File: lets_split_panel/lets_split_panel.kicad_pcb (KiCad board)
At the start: 2 copper layers, 230.5 x 82 mm, 122 parts, among them J1 Speaker, J3 ISP, J5 Speaker, J6 ISP, J7 WS2812>, J8 WS2812>, P2 USB_OTG, P3 >WS2812, P4 Conn_01x04, P5 USB_OTG, P6 >WS2812, P8 Conn_01x04, SW1 Socket, SW10 Socket, SW11 Socket, SW12 Socket, SW13 Socket, SW14 Socket, SW15 Socket, SW16 Socket, SW17 Socket, SW18 Socket, SW19 Socket, SW2 Socket, SW20 Socket, SW21 Socket, SW22 Socket, SW23 Socket, SW24 Socket, SW25 Socket, SW26 Socket, SW27 Socket, SW28 Socket, SW29 Socket, SW3 Socket, SW30 Socket, SW31 Socket, SW32 Socket, SW33 Socket, SW34 Socket, SW35 Socket, SW36 Socket, SW37 Socket, SW38 Socket, SW39 Socket, SW4 Socket, SW40 Socket, SW41 Socket, SW42 Socket, SW43 Socket, SW44 Socket, SW45 Socket, SW46 Socket, SW47 Socket, SW48 Socket, SW5 Socket, SW6 Socket, SW7 Socket, SW8 Socket, SW9 Socket, U1 ATMega32U4, U2 ATMega32U4, Y1 Crystal, Y2 Crystal

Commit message: updated gerbers
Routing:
- net /Right half/col5: track 139.9 -> 140.7 mm

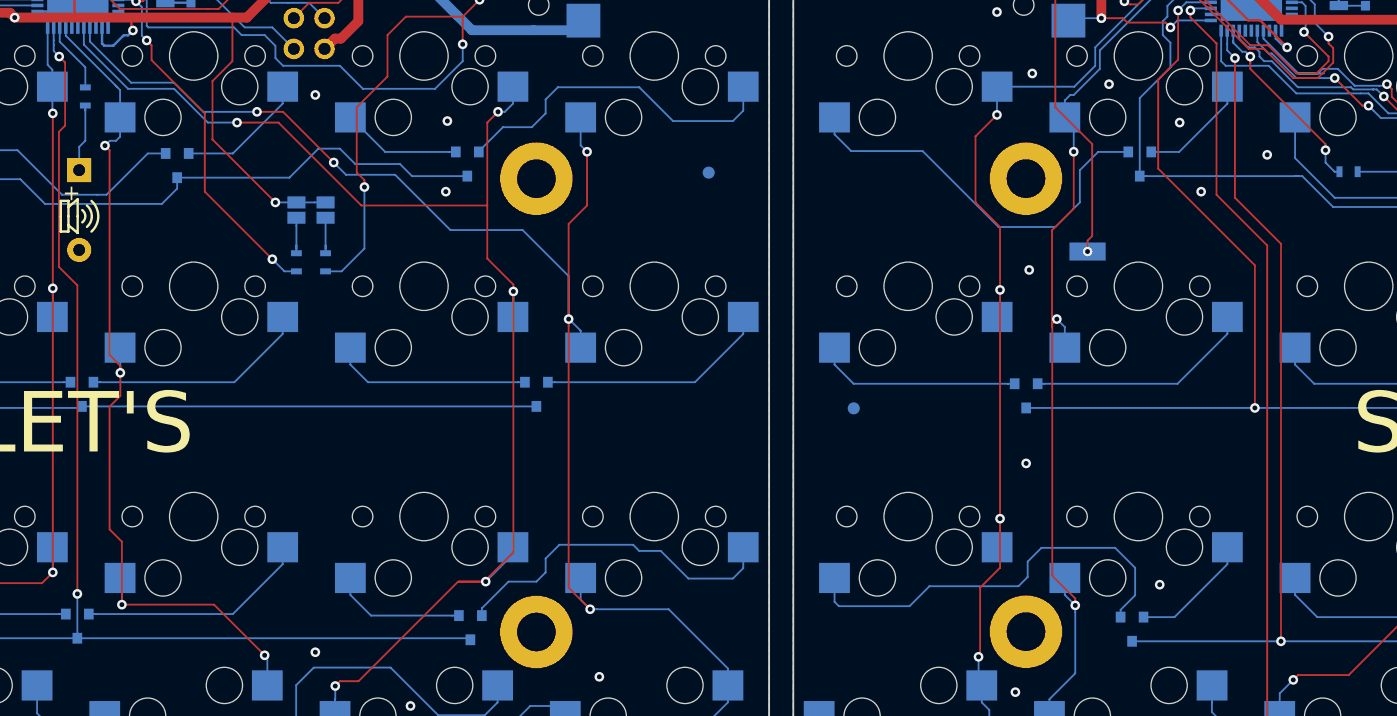
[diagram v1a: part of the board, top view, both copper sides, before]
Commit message: Seperated gerbers on request from board house
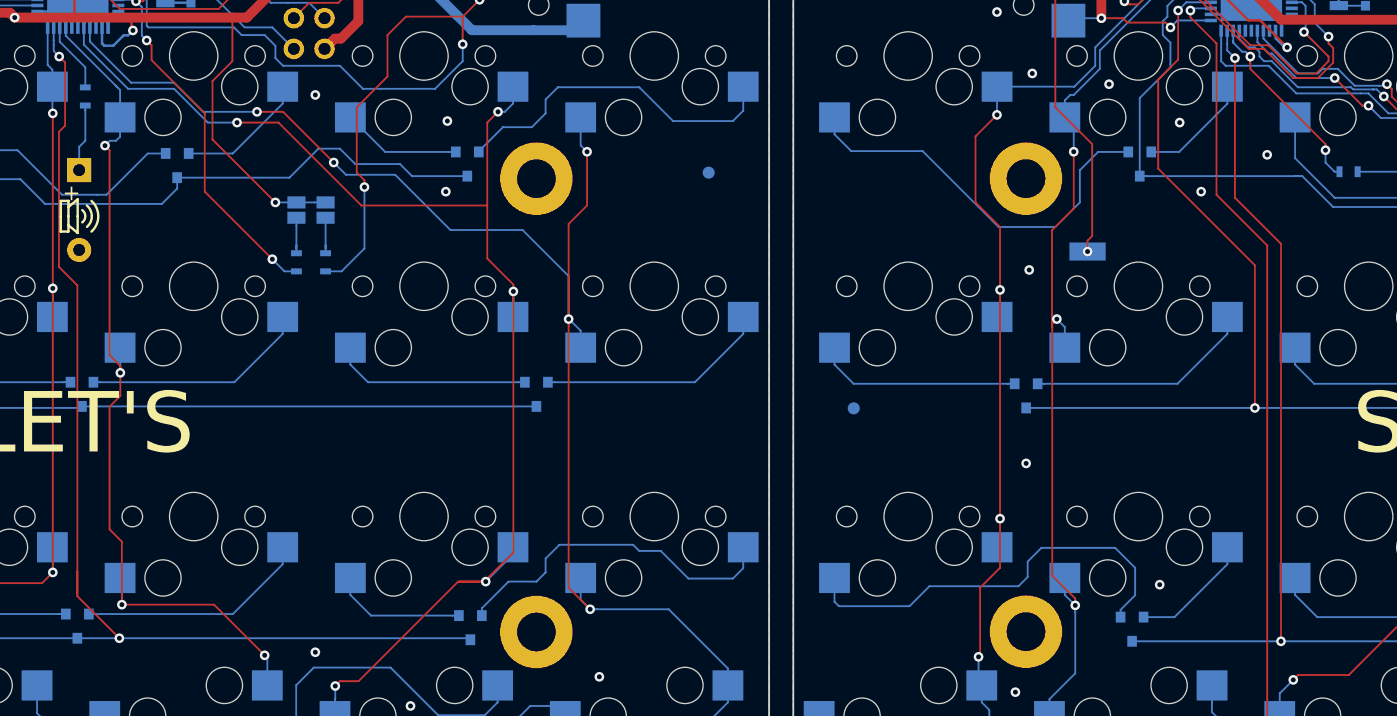
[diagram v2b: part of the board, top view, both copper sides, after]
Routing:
- net /Left half/row2: track 114.1 -> 117.4 mm
- net /Right half/col5: track 140.7 -> 138.6 mm

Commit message: Added PnP files and split gerbers
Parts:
- added FID5: Fiducial, Fiducials:Fiducial_1mm_Dia_2mm_Outer, B.Cu at (143.8, 68.8)
- added FID6: Fiducial, Fiducials:Fiducial_1mm_Dia_2mm_Outer, B.Cu at (27.5, 68.8)
- added G***: LOGO, graphics:kiwi, F.Cu at (203.7, 62.8)
- added G***: LOGO, graphics:kiwi, F.Cu at (67.7, 62.8)
- C2, C3, C6, C7: value 8pF -> 18pF
- FID1, FID2, FID3, FID4: renamed from REF**; value Fiducial_1mm_Dia_2mm_Outer -> Fiducial
- R10, R3: value 200 -> 200R
- Y1, Y2: footprint SeeedOPL-Crystal Oscillator-2016:X2-SMD-3.2X1.5X0.55MM -> Crystals:Crystal_SMD_Abracon_ABM3-2pin_5.0x3.2mm
- moved C6 2.19 mm to (189.8, 68.2)
- moved C7 2.17 mm to (189.8, 65.0)
- moved C2 1.90 mm to (92.0, 68.8)
- moved C3 1.58 mm to (92.0, 64.8)
- moved Y2 1.52 mm to (186.8, 66.5)
- moved Y1 1.03 mm to (89.2, 66.5)
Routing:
- net GND: track 298.2 -> 290.5 mm, vias 41 -> 40
- net Net-(C7-Pad1): track 6.89 -> 10.5 mm
- net Net-(C3-Pad1): track 6.86 -> 9.54 mm
- net Net-(C6-Pad1): track 6.89 -> 8.92 mm
- net Net-(C2-Pad1): track 6.80 -> 8.78 mm
- net /Left half/SDA: track 84.0 -> 85.8 mm
- net /Left half/~Reset: track 24.0 -> 23.4 mm

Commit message: Added BOM
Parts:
- D1, D10, D11, D12, D13, D14, D15, D16, D17, D18, D19, D2, D20, D21, D22, D23, D24, D3, D4, D5, D6, D7, D8, D9: value D_x2_KCom_AAK -> BAV70
- P2, P5: value USB_OTG -> UJ2-MBH-1-SMT
- P4, P8: value Conn_01x04 -> SJ-43514-SMT
- Y1, Y2: value Crystal -> 16MHz
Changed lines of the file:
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@@
       (effects (font (size 1 1) (thickness 0.15)) (justify mirror))
     )
-    (fp_text value USB_OTG (at 0 7.62) (layer B.Fab)
+    (fp_text value UJ2-MBH-1-SMT (at 0 7.62) (layer B.Fab)
       (effects (font (size 1 1) (thickness 0.15)) (justify mirror))
     )
@@
       (effects (font (size 1 1) (thickness 0.15)) (justify mirror))
     )
-    (fp_text value D_x2_KCom_AAK (at 0 -2.5 270) (layer B.Fab)
+    (fp_text value BAV70 (at 0 -2.5 270) (layer B.Fab)
       (effects (font (size 1 1) (thickness 0.15)) (justify mirror))
     )
@@
       (effects (font (size 1 1) (thickness 0.15)) (justify mirror))
     )
-    (fp_text value D_x2_KCom_AAK (at 0 -2.5 270) (layer B.Fab)
+    (fp_text value BAV70 (at 0 -2.5 270) (layer B.Fab)
       (effects (font (size 1 1) (thickness 0.15)) (justify mirror))
     )
@@
       (effects (font (size 1 1) (thickness 0.15)) (justify mirror))
     )
-    (fp_text value Crystal (at 0 -2.8 90) (layer B.Fab)
+    (fp_text value 16MHz (at 0 -2.8 90) (layer B.Fab)
       (effects (font (size 1 1) (thickness 0.15)) (justify mirror))
     )
@@
       (effects (font (size 1 1) (thickness 0.15)) (justify mirror))
     )
-    (fp_text value Conn_01x04 (at 0 -7.747 270) (layer B.Fab)
+    (fp_text value SJ-43514-SMT (at 0 -7.747 270) (layer B.Fab)
       (effects (font (size 1 1) (thickness 0.15)) (justify mirror))
     )
@@
       (effects (font (size 1 1) (thickness 0.15)) (justify mirror))
     )
-    (fp_text value D_x2_KCom_AAK (at 0 -2.5 270) (layer B.Fab)
+    (fp_text value BAV70 (at 0 -2.5 270) (layer B.Fab)
       (effects (font (size 1 1) (thickness 0.15)) (justify mirror))
     )
@@
       (effects (font (size 1 1) (thickness 0.15)) (justify mirror))
     )
-    (fp_text value D_x2_KCom_AAK (at 0 -2.5 270) (layer B.Fab)
+    (fp_text value BAV70 (at 0 -2.5 270) (layer B.Fab)
       (effects (font (size 1 1) (thickness 0.15)) (justify mirror))
     )
@@
       (effects (font (size 1 1) (thickness 0.15)) (justify mirror))
     )
-    (fp_text value D_x2_KCom_AAK (at 0 -2.5 270) (layer B.Fab)
+    (fp_text value BAV70 (at 0 -2.5 270) (layer B.Fab)
       (effects (font (size 1 1) (thickness 0.15)) (justify mirror))
     )
@@
       (effects (font (size 1 1) (thickness 0.15)) (justify mirror))
     )
-    (fp_text value D_x2_KCom_AAK (at 0 -2.5 270) (layer B.Fab)
+    (fp_text value BAV70 (at 0 -2.5 270) (layer B.Fab)
       (effects (font (size 1 1) (thickness 0.15)) (justify mirror))
     )
@@
       (effects (font (size 1 1) (thickness 0.15)) (justify mirror))
     )
-    (fp_text value D_x2_KCom_AAK (at 0 -2.5 270) (layer B.Fab)
+    (fp_text value BAV70 (at 0 -2.5 270) (layer B.Fab)
       (effects (font (size 1 1) (thickness 0.15)) (justify mirror))
     )
@@
       (effects (font (size 1 1) (thickness 0.15)) (justify mirror))
     )
-    (fp_text value D_x2_KCom_AAK (at 0 -2.5 270) (layer B.Fab)
+    (fp_text value BAV70 (at 0 -2.5 270) (layer B.Fab)
       (effects (font (size 1 1) (thickness 0.15)) (justify mirror))
     )
@@
       (effects (font (size 1 1) (thickness 0.15)) (justify mirror))
     )
-    (fp_text value D_x2_KCom_AAK (at 0 -2.5 270) (layer B.Fab)
+    (fp_text value BAV70 (at 0 -2.5 270) (layer B.Fab)
       (effects (font (size 1 1) (thickness 0.15)) (justify mirror))
     )
@@
       (effects (font (size 1 1) (thickness 0.15)) (justify mirror))
     )
-    (fp_text value D_x2_KCom_AAK (at 0 -2.5 270) (layer B.Fab)
+    (fp_text value BAV70 (at 0 -2.5 270) (layer B.Fab)
       (effects (font (size 1 1) (thickness 0.15)) (justify mirror))
     )
@@
       (effects (font (size 1 1) (thickness 0.15)) (justify mirror))
     )
-    (fp_text value D_x2_KCom_AAK (at 0 -2.5 270) (layer B.Fab)
+    (fp_text value BAV70 (at 0 -2.5 270) (layer B.Fab)
       (effects (font (size 1 1) (thickness 0.15)) (justify mirror))
     )
@@
       (effects (font (size 1 1) (thickness 0.15)) (justify mirror))
     )
-    (fp_text value D_x2_KCom_AAK (at 0 -2.5 270) (layer B.Fab)
+    (fp_text value BAV70 (at 0 -2.5 270) (layer B.Fab)
       (effects (font (size 1 1) (thickness 0.15)) (justify mirror))
     )
@@
       (effects (font (size 1 1) (thickness 0.15)) (justify mirror))
     )
-    (fp_text value D_x2_KCom_AAK (at 0 -2.5 270) (layer B.Fab)
+    (fp_text value BAV70 (at 0 -2.5 270) (layer B.Fab)
       (effects (font (size 1 1) (thickness 0.15)) (justify mirror))
     )
@@
       (effects (font (size 1 1) (thickness 0.15)) (justify mirror))
     )
-    (fp_text value D_x2_KCom_AAK (at 0 -2.5 270) (layer B.Fab)
+    (fp_text value BAV70 (at 0 -2.5 270) (layer B.Fab)
       (effects (font (size 1 1) (thickness 0.15)) (justify mirror))
     )
@@
       (effects (font (size 1 1) (thickness 0.15)) (justify mirror))
     )
-    (fp_text value D_x2_KCom_AAK (at 0 -2.5 270) (layer B.Fab)
+    (fp_text value BAV70 (at 0 -2.5 270) (layer B.Fab)
       (effects (font (size 1 1) (thickness 0.15)) (justify mirror))
     )
@@
       (effects (font (size 1 1) (thickness 0.15)) (justify mirror))
     )
-    (fp_text value D_x2_KCom_AAK (at 0 -2.5 270) (layer B.Fab)
+    (fp_text value BAV70 (at 0 -2.5 270) (layer B.Fab)
       (effects (font (size 1 1) (thickness 0.15)) (justify mirror))
     )
@@
       (effects (font (size 1 1) (thickness 0.15)) (justify mirror))
     )
-    (fp_text value D_x2_KCom_AAK (at 0 -2.5 270) (layer B.Fab)
+    (fp_text value BAV70 (at 0 -2.5 270) (layer B.Fab)
       (effects (font (size 1 1) (thickness 0.15)) (justify mirror))
     )
@@
       (effects (font (size 1 1) (thickness 0.15)) (justify mirror))
     )
-    (fp_text value D_x2_KCom_AAK (at 0 -2.5 270) (layer B.Fab)
+    (fp_text value BAV70 (at 0 -2.5 270) (layer B.Fab)
       (effects (font (size 1 1) (thickness 0.15)) (justify mirror))
     )
@@
       (effects (font (size 1 1) (thickness 0.15)) (justify mirror))
     )
-    (fp_text value D_x2_KCom_AAK (at 0 -2.5 270) (layer B.Fab)
+    (fp_text value BAV70 (at 0 -2.5 270) (layer B.Fab)
       (effects (font (size 1 1) (thickness 0.15)) (justify mirror))
     )
@@
       (effects (font (size 1 1) (thickness 0.15)) (justify mirror))
     )
-    (fp_text value D_x2_KCom_AAK (at 0 -2.5 270) (layer B.Fab)
+    (fp_text value BAV70 (at 0 -2.5 270) (layer B.Fab)
       (effects (font (size 1 1) (thickness 0.15)) (justify mirror))
     )
@@
       (effects (font (size 1 1) (thickness 0.15)) (justify mirror))
     )
-    (fp_text value D_x2_KCom_AAK (at 0 -2.5 270) (layer B.Fab)
+    (fp_text value BAV70 (at 0 -2.5 270) (layer B.Fab)
       (effects (font (size 1 1) (thickness 0.15)) (justify mirror))
     )
@@
       (effects (font (size 1 1) (thickness 0.15)) (justify mirror))
     )
-    (fp_text value D_x2_KCom_AAK (at 0 -2.5 270) (layer B.Fab)
+    (fp_text value BAV70 (at 0 -2.5 270) (layer B.Fab)
       (effects (font (size 1 1) (thickness 0.15)) (justify mirror))
     )
@@
       (effects (font (size 1 1) (thickness 0.15)) (justify mirror))
     )
-    (fp_text value USB_OTG (at 0 7.62) (layer B.Fab)
+    (fp_text value UJ2-MBH-1-SMT (at 0 7.62) (layer B.Fab)
       (effects (font (size 1 1) (thickness 0.15)) (justify mirror))
     )
@@
       (effects (font (size 1 1) (thickness 0.15)) (justify mirror))
     )
-    (fp_text value D_x2_KCom_AAK (at 0 -2.5 270) (layer B.Fab)
+    (fp_text value BAV70 (at 0 -2.5 270) (layer B.Fab)
       (effects (font (size 1 1) (thickness 0.15)) (justify mirror))
     )
@@
       (effects (font (size 1 1) (thickness 0.15)) (justify mirror))
     )
-    (fp_text value D_x2_KCom_AAK (at 0 -2.5 270) (layer B.Fab)
+    (fp_text value BAV70 (at 0 -2.5 270) (layer B.Fab)
       (effects (font (size 1 1) (thickness 0.15)) (justify mirror))
     )
@@
       (effects (font (size 1 1) (thickness 0.15)) (justify mirror))
     )
-    (fp_text value Crystal (at 0 -2.8 90) (layer B.Fab)
+    (fp_text value 16MHz (at 0 -2.8 90) (layer B.Fab)
       (effects (font (size 1 1) (thickness 0.15)) (justify mirror))
     )
@@
       (effects (font (size 1 1) (thickness 0.15)) (justify mirror))
     )
-    (fp_text value Conn_01x04 (at 0 -7.747 270) (layer B.Fab)
+    (fp_text value SJ-43514-SMT (at 0 -7.747 270) (layer B.Fab)
       (effects (font (size 1 1) (thickness 0.15)) (justify mirror))
     )
